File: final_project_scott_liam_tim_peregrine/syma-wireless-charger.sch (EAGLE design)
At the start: 38 parts, among them U1 SAMD21E

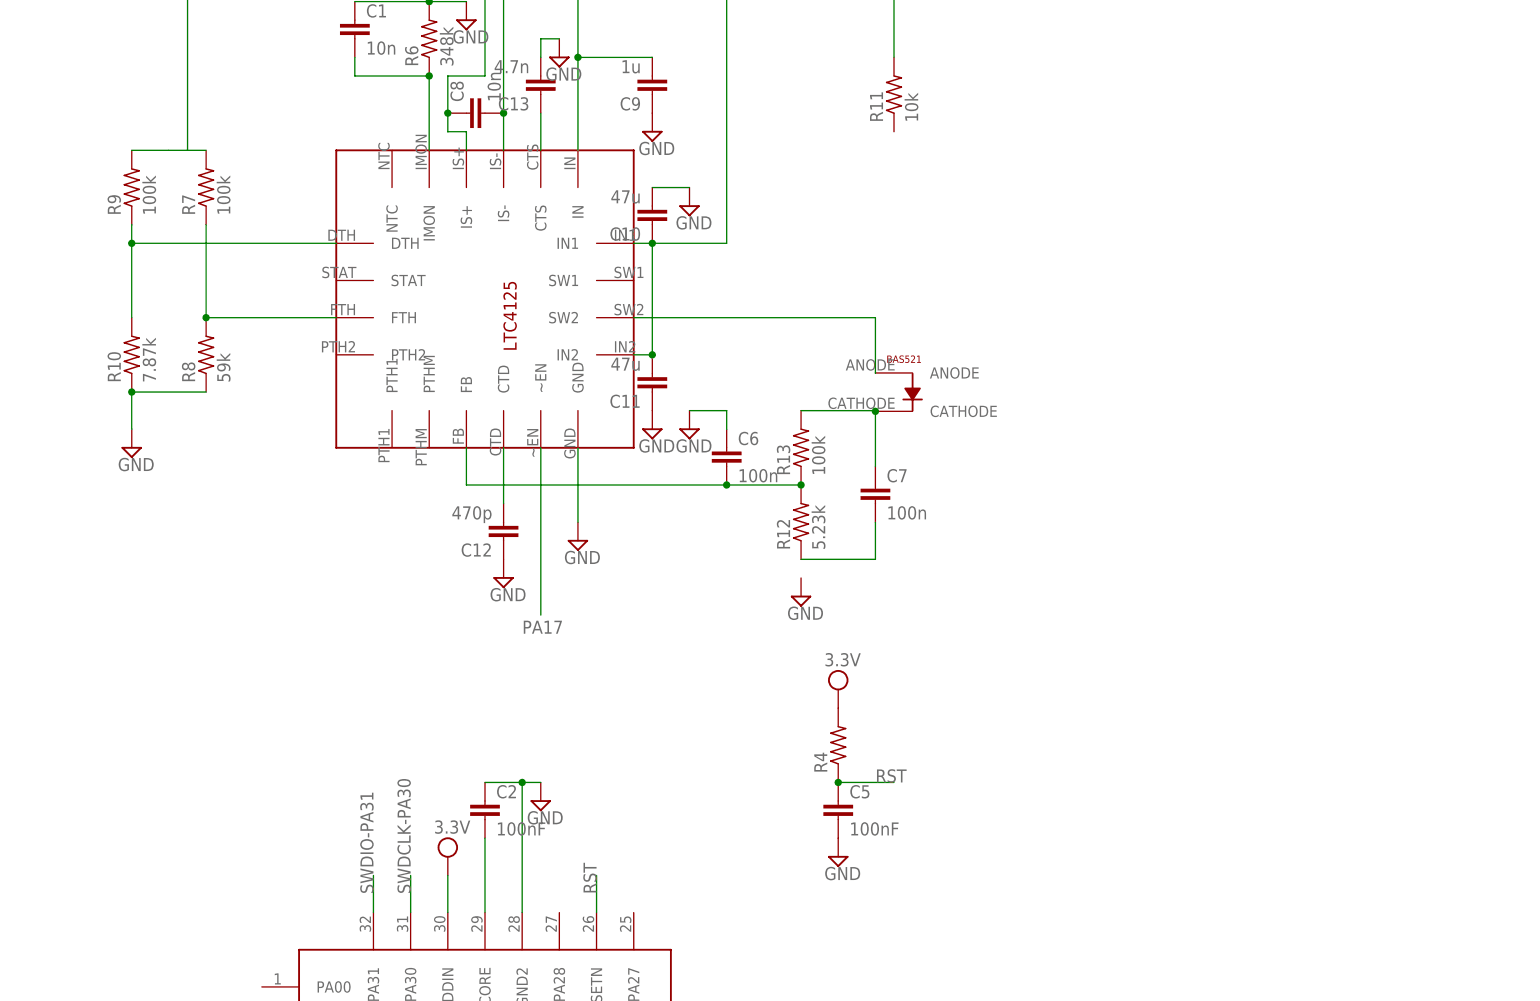
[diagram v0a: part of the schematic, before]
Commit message: removed lock, added light sensors and couple connections to 4125
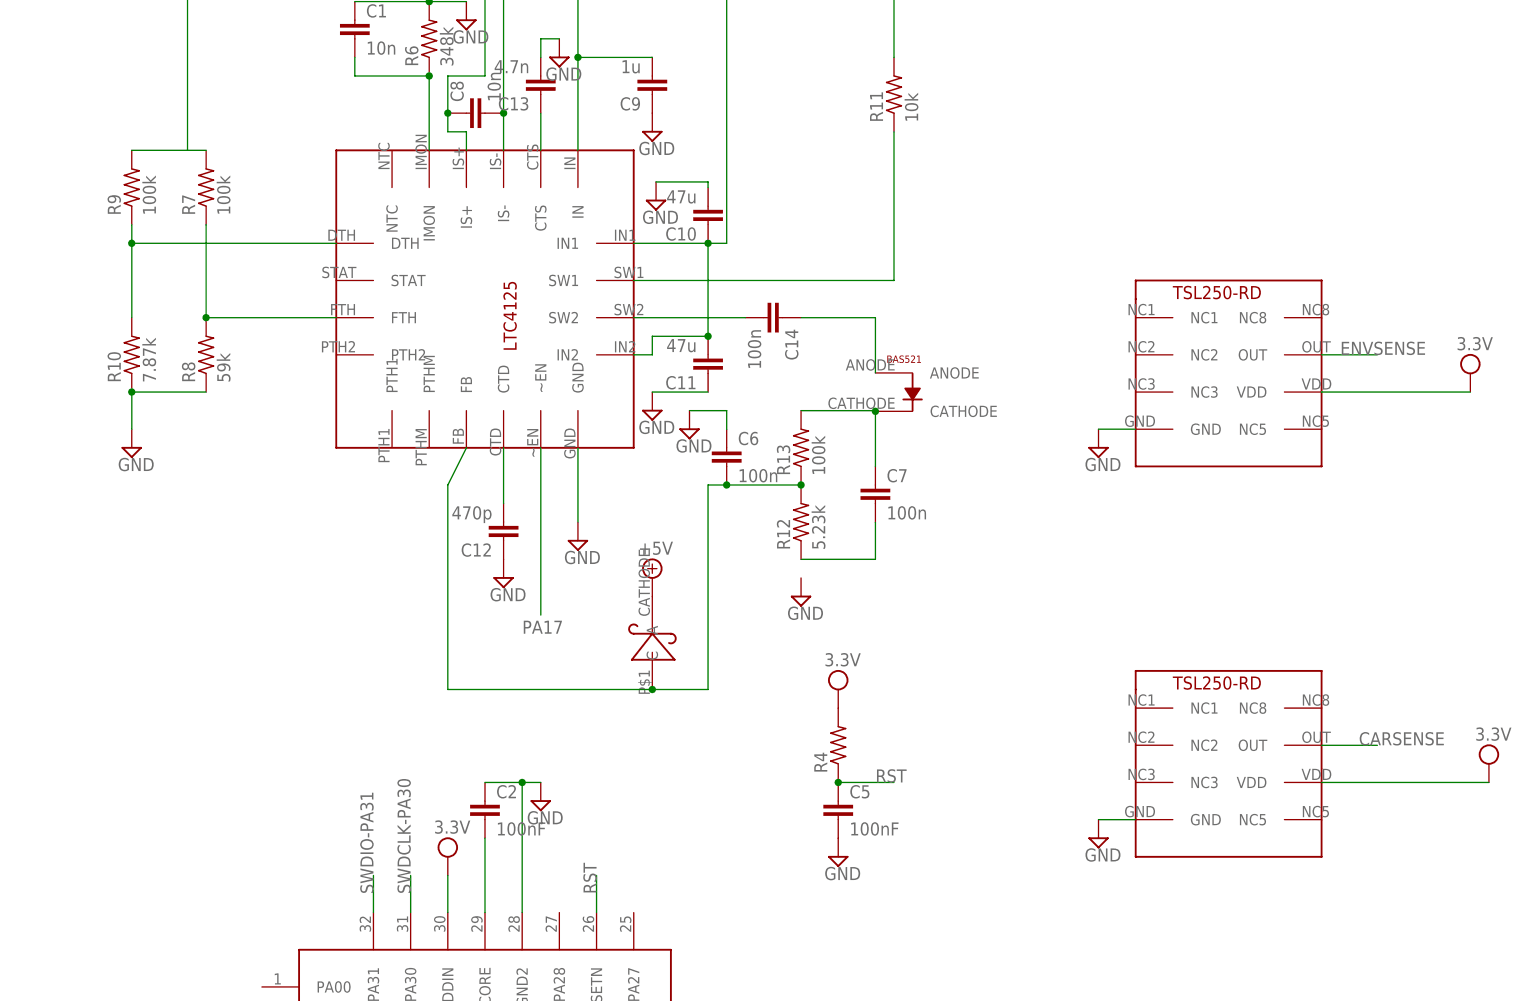
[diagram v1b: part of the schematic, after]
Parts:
- added C14: 100n, rcl:C-EUC0805
- added U$6, U$7: TSL250-RD, foe-scale:TSL250-RD
- added U$8: SCHTKYDIODE-523, foe-scale:SCHTKYDIODE-523
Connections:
- new net 3.3V: U$6.VDD
- new net N$22: C14.2, U$1.SW2
- new net N$7: R11.1, U$1.SW1
- net +5V: now also U$8.C
- net CARSENSE: now also U$6.OUT
- net ENVSENSE: now also U$7.OUT
- net GND: now also U$6.GND, U$7.GND
- net N$12: now also C14.1, U$2.ANODE; no longer U$1.SW2
- net N$9: now also U$8.A
- net VDD: now also U$7.VDD
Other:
- moved on the sheet: C10, C11

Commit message: more 4125 updates
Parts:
- added R14: 2.21k, rcl:R-US_R0805
- added U$9: LTST-C193KGKT_GREEN-LED, foe-scale:LTST-C193KGKT_GREEN-LED
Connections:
- new net N$23: U$1.STAT, U$9.CATHODE
- new net N$26: R14.1, U$9.ANODE
- net GND: now also U$1.PTHM
- net N$20: now also R14.2

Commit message: added receiver board
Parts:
- added R15: 165, resistor:R-US_R0805
- added U$10: PT17-21B_PHOTOTRANSISTOR, foe-scale:PT17-21B_PHOTOTRANSISTOR
- added U$11: 1X02, foe-scale:1X02
- R4: value (none) -> 10k
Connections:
- new net N$28: R15.1, U$10.COLLECTOR
- net GND: now also U$10.EMITTER
- net N$12: now also U$11.P$2
- net N$7: now also U$11.P$1
- net VDD: now also R15.2
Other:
- note added: "HIGH VOLTAGE CAP"
- note added: "Phototransistor for IR LED from car charger"
- note added: "Pins for transmit coil"
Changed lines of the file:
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@@
 <?xml version="1.0" encoding="utf-8"?>
 <!DOCTYPE eagle SYSTEM "eagle.dtd">
-<eagle version="7.5.0">
+<eagle version="7.4.0">
 <drawing>
 <settings>
@@
 <part name="SUPPLY9" library="supply2" deviceset="VDD" device="" value="3.3V"/>
 <part name="SUPPLY10" library="supply2" deviceset="VDD" device="" value="3.3V"/>
-<part name="R4" library="resistor" deviceset="R-US_" device="R0805"/>
+<part name="R4" library="resistor" deviceset="R-US_" device="R0805" value="10k"/>
 <part name="C5" library="resistor" deviceset="C-EU" device="C0805K" value="100nF"/>
 <part name="SUPPLY11" library="supply2" deviceset="GND" device=""/>
@@
 <part name="U$9" library="foe-scale" deviceset="LTST-C193KGKT_GREEN-LED" device=""/>
 <part name="R14" library="rcl" deviceset="R-US_" device="R0805" value="2.21k"/>
+<part name="U$10" library="foe-scale" deviceset="PT17-21B_PHOTOTRANSISTOR" device=""/>
+<part name="SUPPLY34" library="supply2" deviceset="GND" device=""/>
+<part name="R15" library="resistor" deviceset="R-US_" device="R0805" value="165"/>
+<part name="SUPPLY35" library="supply2" deviceset="VDD" device="" value="3.3V"/>
+<part name="U$11" library="foe-scale" deviceset="1X02" device=""/>
 </parts>
 <sheets>
 <sheet>
 <plain>
+<text x="167.64" y="-40.64" size="1.778" layer="91">Phototransistor for IR LED from car charger</text>
+<text x="137.16" y="96.52" size="1.778" layer="91">Pins for transmit coil</text>
+<text x="93.98" y="35.56" size="1.778" layer="91">HIGH VOLTAGE CAP</text>
 </plain>
 <instances>
@@
 <instance part="U$9" gate="G$1" x="10.16" y="81.28"/>
 <instance part="R14" gate="G$1" x="10.16" y="99.822" rot="R90"/>
+<instance part="U$10" gate="G$1" x="208.28" y="-48.26"/>
+<instance part="SUPPLY34" gate="GND" x="208.28" y="-71.12"/>
+<instance part="R15" gate="G$1" x="208.28" y="-22.86" rot="R90"/>
+<instance part="SUPPLY35" gate="G$1" x="208.28" y="-10.16"/>
+<instance part="U$11" gate="G$1" x="137.16" y="88.9"/>
 </instances>
 <busses>
@@
 <pinref part="SUPPLY33" gate="GND" pin="GND"/>
 <wire x1="30.48" y1="40.64" x2="30.48" y2="35.56" width="0.1524" layer="91"/>
+</segment>
+<segment>
+<pinref part="U$10" gate="G$1" pin="EMITTER"/>
+<wire x1="208.28" y1="-60.96" x2="208.28" y2="-68.58" width="0.1524" layer="91"/>
+<pinref part="SUPPLY34" gate="GND" pin="GND"/>
 </segment>
 </net>
@@
 <wire x1="152.4" y1="48.26" x2="172.72" y2="48.26" width="0.1524" layer="91"/>
 <pinref part="SUPPLY31" gate="G$1" pin="VDD"/>
+</segment>
+<segment>
+<pinref part="R15" gate="G$1" pin="2"/>
+<wire x1="208.28" y1="-17.78" x2="208.28" y2="-12.7" width="0.1524" layer="91"/>
+<pinref part="SUPPLY35" gate="G$1" pin="VDD"/>
 </segment>
 </net>
@@
 <wire x1="81.28" y1="58.42" x2="91.44" y2="58.42" width="0.1524" layer="91"/>
 <pinref part="U$2" gate="G$1" pin="ANODE"/>
+<wire x1="91.44" y1="58.42" x2="116.84" y2="58.42" width="0.1524" layer="91"/>
+<wire x1="116.84" y1="58.42" x2="116.84" y2="86.36" width="0.1524" layer="91"/>
+<junction x="91.44" y="58.42"/>
+<pinref part="U$11" gate="G$1" pin="P$2"/>
+<wire x1="116.84" y1="86.36" x2="137.16" y2="86.36" width="0.1524" layer="91"/>
 </segment>
 </net>
@@
 <pinref part="R11" gate="G$1" pin="1"/>
 <wire x1="93.98" y1="63.5" x2="93.98" y2="83.82" width="0.1524" layer="91"/>
+<wire x1="93.98" y1="63.5" x2="109.22" y2="63.5" width="0.1524" layer="91"/>
+<wire x1="109.22" y1="63.5" x2="109.22" y2="91.44" width="0.1524" layer="91"/>
+<junction x="93.98" y="63.5"/>
+<pinref part="U$11" gate="G$1" pin="P$1"/>
+<wire x1="109.22" y1="91.44" x2="137.16" y2="91.44" width="0.1524" layer="91"/>
 </segment>
 </net>
@@
 </segment>
 </net>
+<net name="N$28" class="0">
+<segment>
+<pinref part="R15" gate="G$1" pin="1"/>
+<pinref part="U$10" gate="G$1" pin="COLLECTOR"/>
+<wire x1="208.28" y1="-27.94" x2="208.28" y2="-35.56" width="0.1524" layer="91"/>
+</segment>
+</net>

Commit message: fixed green LED symbol
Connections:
- net N$23: no longer U$9.CATHODE
- net N$26: no longer U$9.ANODE
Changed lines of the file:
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@@
 <?xml version="1.0" encoding="utf-8"?>
 <!DOCTYPE eagle SYSTEM "eagle.dtd">
-<eagle version="7.4.0">
+<eagle version="7.5.0">
 <drawing>
 <settings>
@@
 <part name="SUPPLY32" library="supply2" deviceset="+5V" device=""/>
 <part name="SUPPLY33" library="supply2" deviceset="GND" device=""/>
-<part name="U$9" library="foe-scale" deviceset="LTST-C193KGKT_GREEN-LED" device=""/>
 <part name="R14" library="rcl" deviceset="R-US_" device="R0805" value="2.21k"/>
 <part name="U$10" library="foe-scale" deviceset="PT17-21B_PHOTOTRANSISTOR" device=""/>
@@
 <part name="SUPPLY35" library="supply2" deviceset="VDD" device="" value="3.3V"/>
 <part name="U$11" library="foe-scale" deviceset="1X02" device=""/>
+<part name="U$9" library="foe-scale" deviceset="LTST-C193KGKT_GREEN-LED" device=""/>
 </parts>
 <sheets>
@@
 <instance part="SUPPLY32" gate="+5V" x="60.96" y="22.86"/>
 <instance part="SUPPLY33" gate="GND" x="30.48" y="33.02" rot="MR0"/>
-<instance part="U$9" gate="G$1" x="10.16" y="81.28"/>
 <instance part="R14" gate="G$1" x="10.16" y="99.822" rot="R90"/>
 <instance part="U$10" gate="G$1" x="208.28" y="-48.26"/>
@@
 <instance part="SUPPLY35" gate="G$1" x="208.28" y="-10.16"/>
 <instance part="U$11" gate="G$1" x="137.16" y="88.9"/>
+<instance part="U$9" gate="G$1" x="10.16" y="83.82"/>
 </instances>
 <busses>
@@
 <net name="N$23" class="0">
 <segment>
-<pinref part="U$9" gate="G$1" pin="CATHODE"/>
-<wire x1="10.16" y1="73.66" x2="10.16" y2="63.5" width="0.1524" layer="91"/>
+<wire x1="10.16" y1="81.28" x2="10.16" y2="63.5" width="0.1524" layer="91"/>
 <pinref part="U$1" gate="G$1" pin="STAT"/>
 <wire x1="10.16" y1="63.5" x2="17.78" y2="63.5" width="0.1524" layer="91"/>
@@
 <segment>
 <pinref part="R14" gate="G$1" pin="1"/>
-<pinref part="U$9" gate="G$1" pin="ANODE"/>
-<wire x1="10.16" y1="94.742" x2="10.16" y2="91.44" width="0.1524" layer="91"/>
-</segment>
-</net>
+<wire x1="10.16" y1="94.742" x2="10.16" y2="88.138" width="0.1524" layer="91"/>
+</segment>
+</net>

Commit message: started transmitter layout
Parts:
- removed R1: (no value), resistor:R-US_R0805
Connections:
- removed net N$26: R14.1
- removed net N$28: R15.1, U$10.COLLECTOR
- net ALIGNED: now also R15.1, U$10.COLLECTOR
- net GND: now also C7.2, R12.1
- net N$11: now also R14.1, U$9.A; no longer C7.2, R12.1
- net N$23: now also U$9.C
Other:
- note added: "ALIGNED"
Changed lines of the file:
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@@
 <part name="U1" library="foe-scale" deviceset="SAMD21E" device=""/>
 <part name="DBG1" library="foe-scale" deviceset="DEBUGHEAD" device=""/>
-<part name="R1" library="resistor" deviceset="R-US_" device="R0805"/>
 <part name="C2" library="resistor" deviceset="C-EU" device="C0805K" value="100nF"/>
 <part name="U2" library="foe-scale" deviceset="3.3V_AS1363" device=""/>
@@
 <text x="137.16" y="96.52" size="1.778" layer="91">Pins for transmit coil</text>
 <text x="93.98" y="35.56" size="1.778" layer="91">HIGH VOLTAGE CAP</text>
+<text x="191.262" y="-32.004" size="1.778" layer="91">ALIGNED</text>
 </plain>
 <instances>
@@
 <instance part="U1" gate="G$1" x="22.86" y="-35.56"/>
 <instance part="DBG1" gate="G$1" x="-76.2" y="-48.26" rot="R270"/>
-<instance part="R1" gate="G$1" x="-55.88" y="48.26"/>
 <instance part="C2" gate="G$1" x="38.1" y="-7.62"/>
 <instance part="U2" gate="AS1363" x="-73.66" y="15.24"/>
@@
 <instance part="SUPPLY35" gate="G$1" x="208.28" y="-10.16"/>
 <instance part="U$11" gate="G$1" x="137.16" y="88.9"/>
-<instance part="U$9" gate="G$1" x="10.16" y="83.82"/>
+<instance part="U$9" gate="G$1" x="7.62" y="78.74"/>
 </instances>
 <busses>
@@
 <wire x1="208.28" y1="-60.96" x2="208.28" y2="-68.58" width="0.1524" layer="91"/>
 <pinref part="SUPPLY34" gate="GND" pin="GND"/>
+</segment>
+<segment>
+<pinref part="C7" gate="G$1" pin="2"/>
+<wire x1="91.44" y1="30.48" x2="91.44" y2="25.4" width="0.1524" layer="91"/>
+<pinref part="R12" gate="G$1" pin="1"/>
+<wire x1="91.44" y1="25.4" x2="81.28" y2="25.4" width="0.1524" layer="91"/>
+<pinref part="SUPPLY15" gate="GND" pin="GND"/>
+<wire x1="81.28" y1="22.86" x2="81.28" y2="25.4" width="0.1524" layer="91"/>
+<junction x="81.28" y="25.4"/>
 </segment>
 </net>
@@
 </segment>
 </net>
-<net name="N$11" class="0">
-<segment>
-<pinref part="C7" gate="G$1" pin="2"/>
-<wire x1="91.44" y1="30.48" x2="91.44" y2="25.4" width="0.1524" layer="91"/>
-<pinref part="R12" gate="G$1" pin="1"/>
-<wire x1="91.44" y1="25.4" x2="81.28" y2="25.4" width="0.1524" layer="91"/>
-</segment>
-</net>
 <net name="N$12" class="0">
 <segment>
@@
 <wire x1="7.62" y1="-48.26" x2="-7.62" y2="-48.26" width="0.1524" layer="91"/>
 <label x="-7.62" y="-48.26" size="1.778" layer="95"/>
+</segment>
+<segment>
+<pinref part="R15" gate="G$1" pin="1"/>
+<pinref part="U$10" gate="G$1" pin="COLLECTOR"/>
+<wire x1="208.28" y1="-27.94" x2="208.28" y2="-33.02" width="0.1524" layer="91"/>
+<wire x1="208.28" y1="-33.02" x2="208.28" y2="-35.56" width="0.1524" layer="91"/>
+<wire x1="208.28" y1="-33.02" x2="193.04" y2="-33.02" width="0.1524" layer="91"/>
+<junction x="208.28" y="-33.02"/>
 </segment>
 </net>
@@
 <net name="N$23" class="0">
 <segment>
-<wire x1="10.16" y1="81.28" x2="10.16" y2="63.5" width="0.1524" layer="91"/>
 <pinref part="U$1" gate="G$1" pin="STAT"/>
 <wire x1="10.16" y1="63.5" x2="17.78" y2="63.5" width="0.1524" layer="91"/>
-</segment>
-</net>
-<net name="N$26" class="0">
+<pinref part="U$9" gate="G$1" pin="C"/>
+<wire x1="10.16" y1="73.66" x2="10.16" y2="63.5" width="0.1524" layer="91"/>
+</segment>
+</net>
+<net name="N$11" class="0">
 <segment>
 <pinref part="R14" gate="G$1" pin="1"/>
-<wire x1="10.16" y1="94.742" x2="10.16" y2="88.138" width="0.1524" layer="91"/>
-</segment>
-</net>
-<net name="N$28" class="0">
-<segment>
-<pinref part="R15" gate="G$1" pin="1"/>
-<pinref part="U$10" gate="G$1" pin="COLLECTOR"/>
-<wire x1="208.28" y1="-27.94" x2="208.28" y2="-35.56" width="0.1524" layer="91"/>
-</segment>
-</net>
+<pinref part="U$9" gate="G$1" pin="A"/>
+<wire x1="10.16" y1="94.742" x2="10.16" y2="83.82" width="0.1524" layer="91"/>
+</segment>
+</net>
